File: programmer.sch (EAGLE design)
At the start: 14 parts, among them U1 FT232R, X1 53261-06

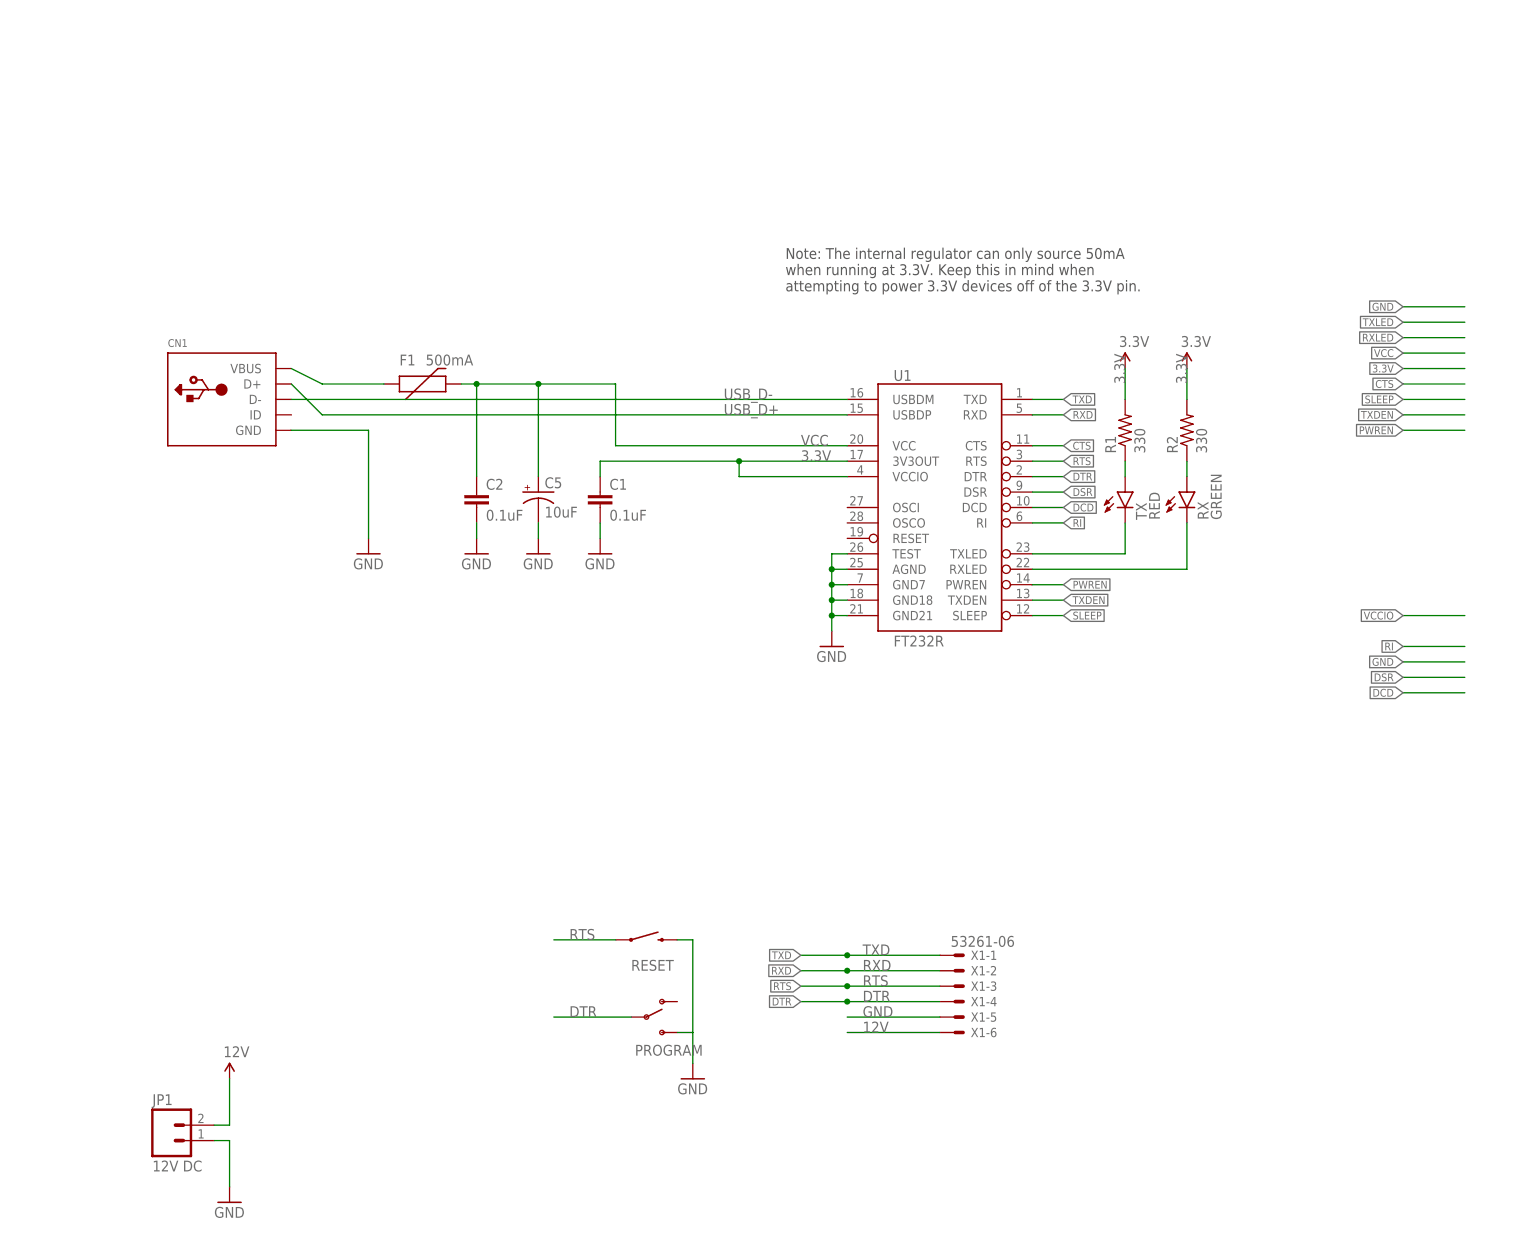
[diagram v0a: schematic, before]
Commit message: Made mofications to schematics for readability
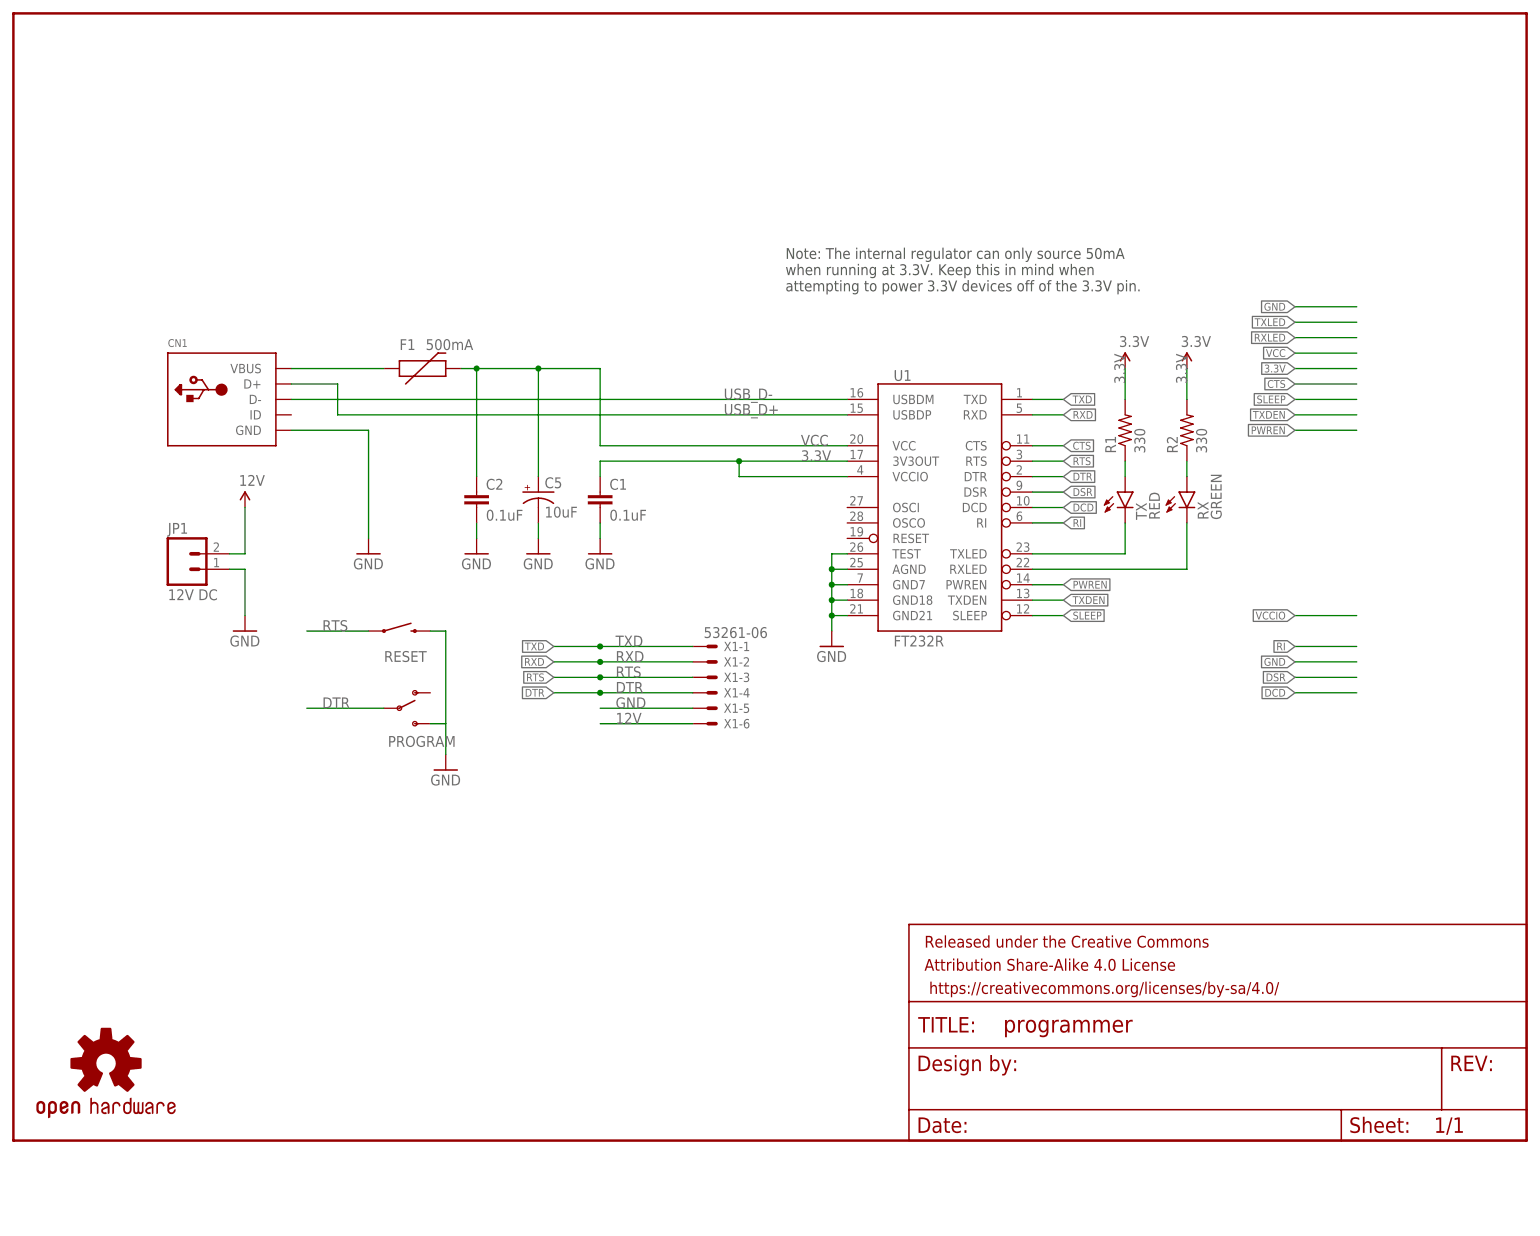
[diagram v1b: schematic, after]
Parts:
- added FRAME1: (no value), SparkFun-Aesthetics:FRAME-LETTERNO_PACKAGE
- added LOGO1: OSHW-LOGOS, SparkFun-Aesthetics:OSHW-LOGOS
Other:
- moved on the sheet: F1, JP1, PROGRAM, RESET, X1-1, X1-2, X1-3, X1-4, X1-5, X1-6

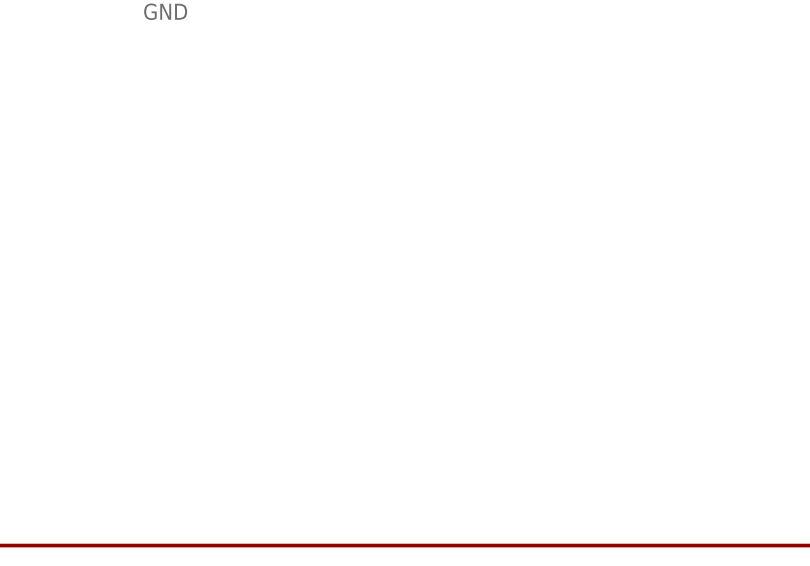
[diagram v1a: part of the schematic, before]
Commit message: Revision of programmer board to include a SMD 6 pin FTDI header.
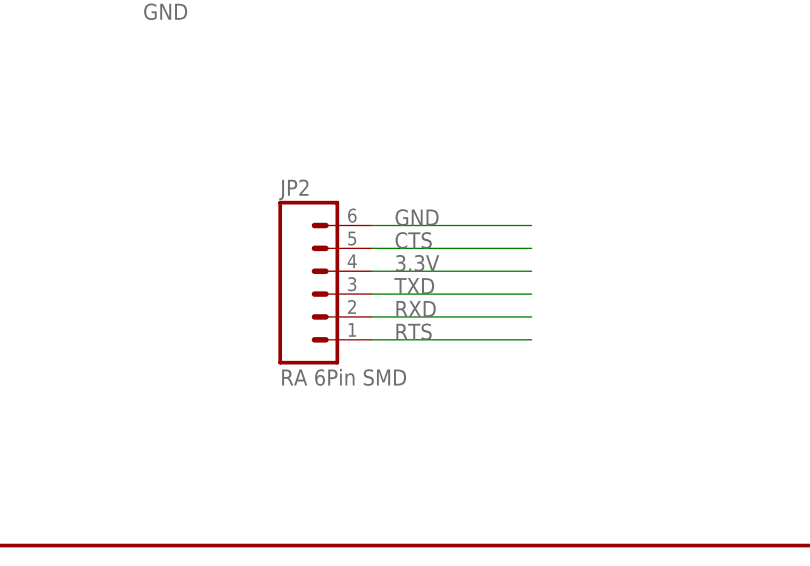
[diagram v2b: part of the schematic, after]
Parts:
- added JP2: RA 6Pin SMD, SparkFun-Connectors:M06SMD
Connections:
- net 3.3V: now also JP2.4
- net CTS: now also JP2.5
- net GND: now also JP2.6
- net RTS: now also JP2.1
- net RXD: now also JP2.2
- net TXD: now also JP2.3
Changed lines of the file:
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@@
 <part name="LOGO1" library="SparkFun-Aesthetics" deviceset="OSHW-LOGO" device="S"/>
 <part name="FRAME1" library="SparkFun-Aesthetics" deviceset="FRAME-LETTER" device="NO_PACKAGE"/>
+<part name="JP2" library="SparkFun-Connectors" deviceset="M06" device="SMD" value="RA 6Pin SMD"/>
 </parts>
 <sheets>
@@
 <instance part="FRAME1" gate="G$1" x="-114.3" y="30.48"/>
 <instance part="FRAME1" gate="V" x="33.02" y="30.48"/>
+<instance part="JP2" gate="G$1" x="-25.4" y="58.42"/>
 </instances>
 <busses>
@@
 <pinref part="GND4" gate="1" pin="GND"/>
 </segment>
+<segment>
+<pinref part="JP2" gate="G$1" pin="6"/>
+<wire x1="-20.32" y1="66.04" x2="-2.54" y2="66.04" width="0.1524" layer="91"/>
+<label x="-17.78" y="66.04" size="1.778" layer="95"/>
+</segment>
 </net>
 <net name="12V" class="0">
@@
 <label x="78.74" y="154.94" size="1.778" layer="95" rot="R90"/>
 <pinref part="SUPPLY3" gate="G$1" pin="3.3V"/>
+</segment>
+<segment>
+<pinref part="JP2" gate="G$1" pin="4"/>
+<wire x1="-20.32" y1="60.96" x2="-2.54" y2="60.96" width="0.1524" layer="91"/>
+<label x="-17.78" y="60.96" size="1.778" layer="95"/>
 </segment>
 </net>
@@
 <junction x="-17.78" y="111.76"/>
 </segment>
+<segment>
+<pinref part="JP2" gate="G$1" pin="3"/>
+<wire x1="-2.54" y1="58.42" x2="-20.32" y2="58.42" width="0.1524" layer="91"/>
+<label x="-17.78" y="58.42" size="1.778" layer="95"/>
+</segment>
 </net>
 <net name="RXD" class="0">
@@
 <junction x="-17.78" y="109.22"/>
 </segment>
+<segment>
+<pinref part="JP2" gate="G$1" pin="2"/>
+<wire x1="-20.32" y1="55.88" x2="-2.54" y2="55.88" width="0.1524" layer="91"/>
+<label x="-17.78" y="55.88" size="1.778" layer="95"/>
+</segment>
 </net>
 <net name="RTS" class="0">
@@
 <label x="-63.5" y="114.3" size="1.778" layer="95"/>
 </segment>
+<segment>
+<pinref part="JP2" gate="G$1" pin="1"/>
+<wire x1="-2.54" y1="53.34" x2="-20.32" y2="53.34" width="0.1524" layer="91"/>
+<label x="-17.78" y="53.34" size="1.778" layer="95"/>
+</segment>
 </net>
 <net name="CTS" class="0">
@@
 <label x="96.52" y="154.94" size="1.27" layer="95" rot="R180" xref="yes"/>
 </segment>
-</net>
+<segment>
+<pinref part="JP2" gate="G$1" pin="5"/>
+<wire x1="-2.54" y1="63.5" x2="-20.32" y2="63.5" width="0.1524" layer="91"/>
+<label x="-17.78" y="63.5" size="1.778" layer="95"/>
+</segment>
+</net>

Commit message: Changed to CH340G + Crystal instead of FT232RL Resolves #4. Using 12 Volt Barrel Jack Resolves #3. Moved to Omron 10xxx switches instead of slider, Resolves #1
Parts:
- removed C1: 0.1uF, SparkFun-Passives:CAP1206
- removed JP1: 12V DC, SparkFun-Connectors:M02JST-PTH-VERT
- removed R1, R2: 330, SparkFun-Passives:RESISTOR1206
- removed RX: GREEN, SparkFun-LED:LED1206
- removed TX: RED, SparkFun-LED:LED1206
- removed U1: FT232R, SparkFun:FT232RLSSOP
- added C3: 0.1uF, rcl:C-EUC1206K
- added C4, C6: 22pf, SparkFun-Capacitors:CAP1206
- added JP3: POWER_JACKPTH_LOCK, SparkFun-Connectors:POWER_JACKPTH_LOCK
- added U$1: CH340G, CH340G-USB-SERIAL:CH340G
- added Y1: 12mhz, SparkFun-FreqCtrl:CRYSTALSMD
- PROGRAM: value (none) -> SWITCH-MOMENTARY-2PTH; device SparkFun-Electromechanical:SWITCH-SPDT-SMD-A -> SparkFun-Electromechanical:SWITCH-MOMENTARY-2PTH
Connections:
- removed net DCD: U1.DCD
- removed net DSR: U1.DSR
- removed net DTR: PROGRAM.P, U1.DTR, X1-4.S
- removed net N$1: R1.1, TX.A
- removed net N$2: R2.1, RX.A
- removed net PWREN: U1.PWREN
- removed net RI: U1.RI
- removed net RTS: JP2.1, RESET.1, U1.RTS, X1-3.S
- removed net RXLED: RX.C, U1.RXLED
- removed net SLEEP: U1.SLEEP
- removed net TXDEN: U1.TXDEN
- removed net TXLED: TX.C, U1.TXLED
- new net GPIO0: PROGRAM.1, X1-4.S
- new net OSCI: C4.1, U$1.XI, Y1.1
- new net OSCO: C6.1, U$1.XO, Y1.2
- new net RESET: JP2.1, RESET.1, X1-3.S
- new net RX: U$1.TX
- new net TX: U$1.RX
- net 12V: now also JP3.PWR; no longer JP1.2
- net 3.3V: now also C3.1, U$1.V3; no longer C1.1, R1.2, R2.2, U1.3V3OUT, U1.VCCIO
- net CTS: now also U$1.CTS; no longer U1.CTS
- net GND: now also C3.2, C4.2, C6.2, JP3.GND, JP3.GNDBREAK, PROGRAM.2, U$1.GND; no longer C1.2, JP1.1, PROGRAM.S, U1.AGND, U1.GND18, U1.GND21, U1.GND7, U1.TEST
- net RXD: no longer U1.RXD
- net TXD: no longer U1.TXD
- net USB_D+: now also U$1.D+; no longer U1.USBDP
- net USB_D-: now also U$1.D-; no longer U1.USBDM
- net VCC: now also U$1.VCC; no longer U1.VCC
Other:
- note removed: "Note: The internal regulator can only source 50mA when running at 3.3V. Keep this in mind when attempting to power 3.3V devices off of the 3.3V pin."
